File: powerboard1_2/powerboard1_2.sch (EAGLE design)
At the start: 132 parts, among them Q1 IPP80P03P4L04AKSA1, Q2 2N4401TFR, Q3 2N4401TFR, Q4 2N4401TFR, U1 UWQ-12/20-T48NTB-C, U2 UWE-5/20-Q48NB-C, U3 UWE-3.3/30-Q48NB-C

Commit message: Changed converters to ones that have input voltage range of 9V to 36V; Reduced length by about 0.5"
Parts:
- U1: value UWQ-12/20-T48NTB-C -> UWE-12/10-Q12PB-C; device New Power Board Library:UWQ-12/20-T48NTB-C -> New Power Board Library:UWE-12/10-Q12PB-C
- U2: value UWE-5/20-Q48NB-C -> UWE-5/15-Q12PB-C; device New Power Board Library:UWE-5/20-Q48NB-C -> New Power Board Library:UWE-5/15-Q12PB-C
- U3: value UWE-3.3/30-Q48NB-C -> UWE-3.3/20-Q12PB-C; device New Power Board Library:UWE-3.3/30-Q48NB-C -> New Power Board Library:UWE-3.3/20-Q12PB-C
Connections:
- new net N$15: U3.+VIN
- net 12V+SENSE: now also R5.1; no longer R11.2
- net 12V-SENSE: now also JP8.5, JP8.6, R13.2, U1.+SEN; no longer JP8.1, JP8.2, R3.1, U1.+SENSE
- net 3V3+SENSE: now also R3.1; no longer R13.2
- net 3V3-SENSE: now also JP8.1, JP8.2, R11.2; no longer JP8.5, JP8.6, R5.1
- net 5V+SENSE: now also R4.1; no longer R12.2
- net 5V-SENSE: now also R12.2; no longer R4.1
- net GND: now also U1.-SEN; no longer U1.-SENSE
- net N$12: no longer U3.+VIN

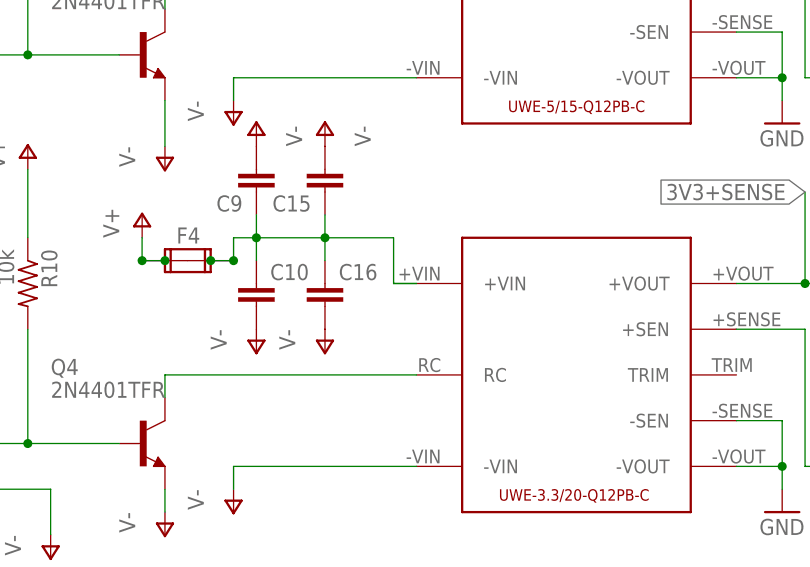
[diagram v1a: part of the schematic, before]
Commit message: Fixed connection issue on 3.3V converter
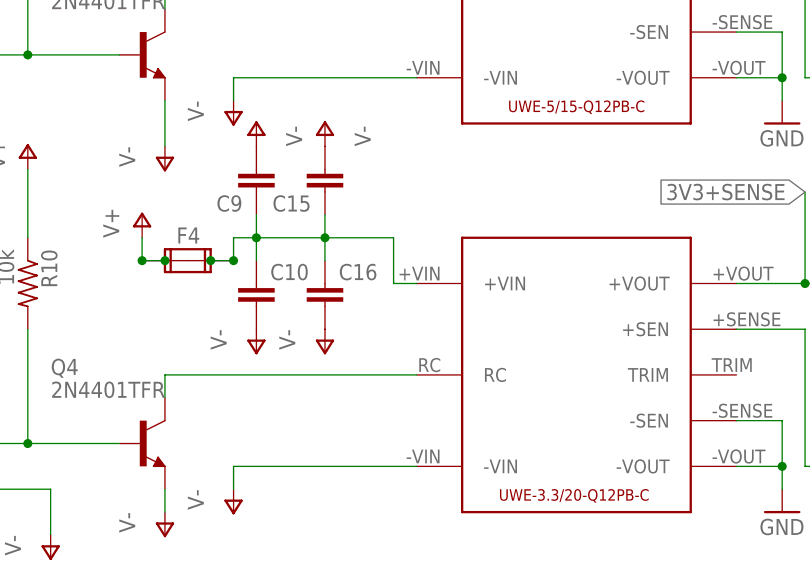
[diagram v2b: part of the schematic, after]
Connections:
- removed net N$15: U3.+VIN
- net N$12: now also U3.+VIN
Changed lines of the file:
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@@
-</segment>
-</net>
-<net name="N$15" class="0">
-<segment>
-<wire x1="116.84" y1="154.94" x2="119.38" y2="154.94" width="0.1524" layer="91"/>
-<pinref part="U3" gate="G$1" pin="+VIN"/>
 </segment>
 </net>
@@
 <wire x1="101.6" y1="160.02" x2="109.22" y2="160.02" width="0.1524" layer="91"/>
 <wire x1="109.22" y1="160.02" x2="116.84" y2="160.02" width="0.1524" layer="91"/>
-<wire x1="116.84" y1="154.94" x2="119.38" y2="154.94" width="0.1524" layer="91"/>
 <wire x1="116.84" y1="160.02" x2="116.84" y2="154.94" width="0.1524" layer="91"/>
 <pinref part="C9" gate="G$1" pin="1"/>
@@
 <junction x="109.22" y="160.02"/>
 <junction x="99.06" y="157.48"/>
+<pinref part="U3" gate="G$1" pin="+VIN"/>
+<wire x1="116.84" y1="154.94" x2="119.38" y2="154.94" width="0.1524" layer="91"/>
 </segment>
 </net>

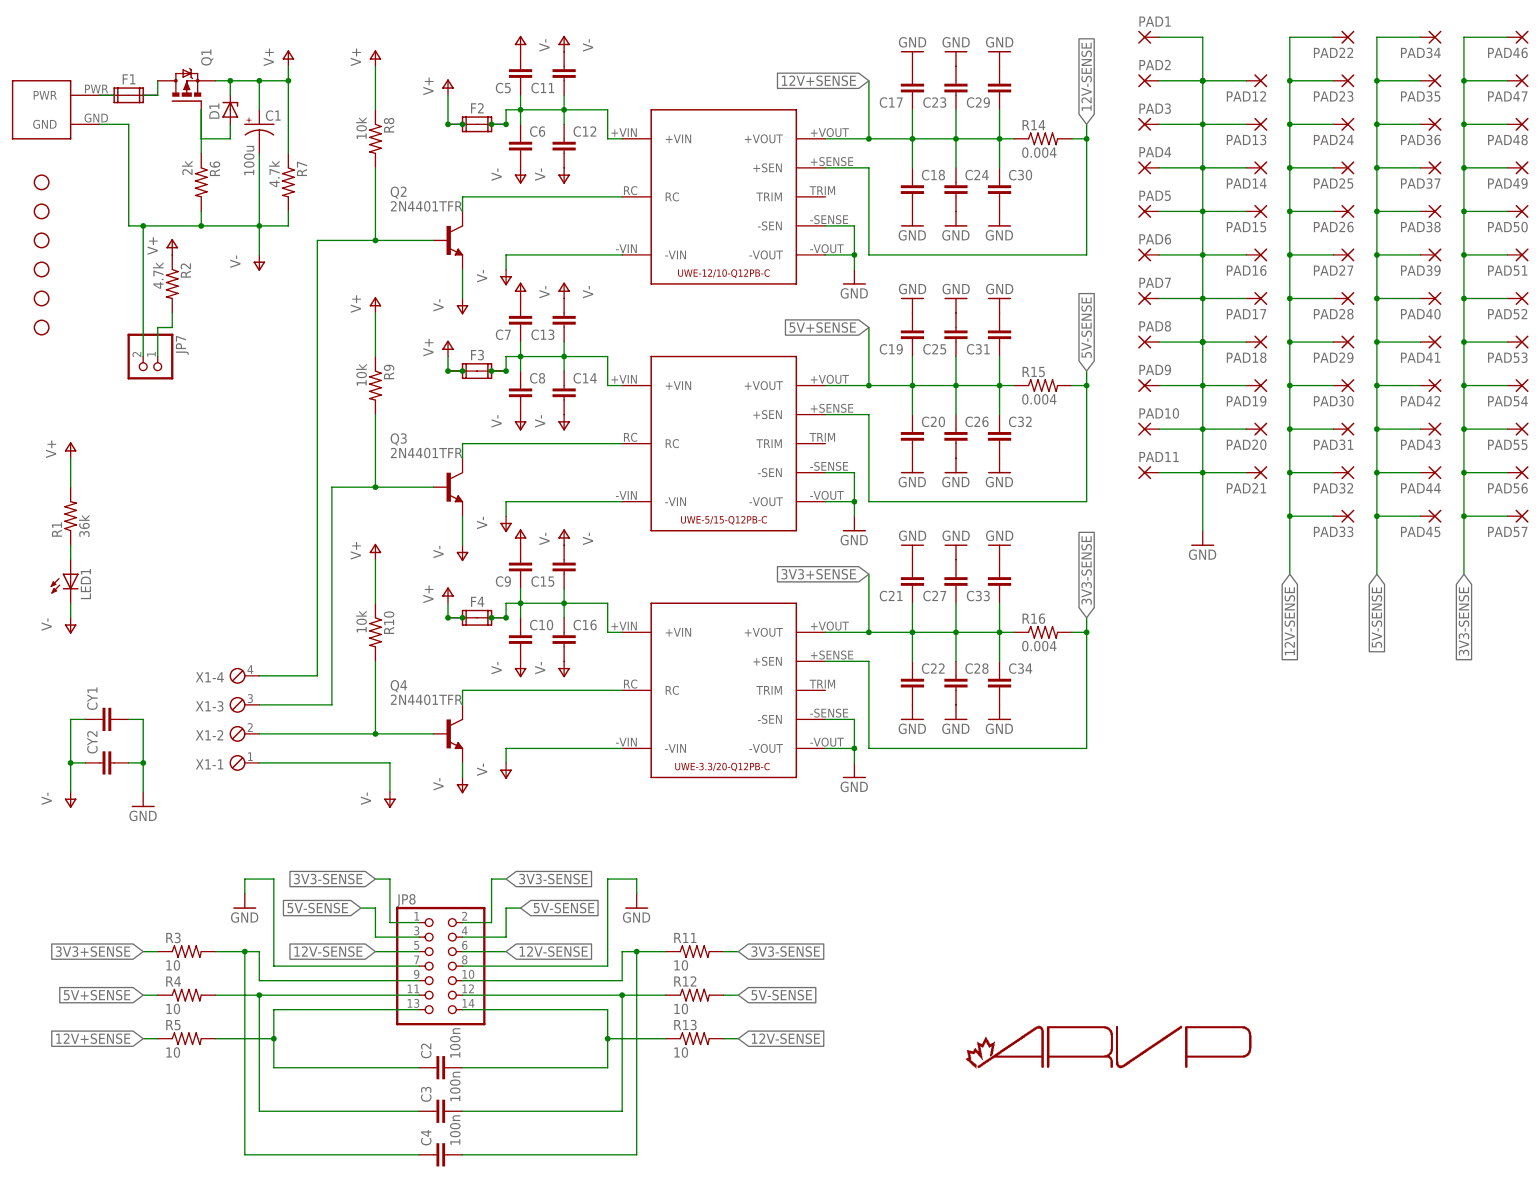
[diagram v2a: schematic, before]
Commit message: Added 2 pin header for global on/off switch; Changed on/off terminal block to 2x3 90 degree pin header; Added LED indicators on each rail; Reduced number of output wire pads; Changed battery connection to screw terminal
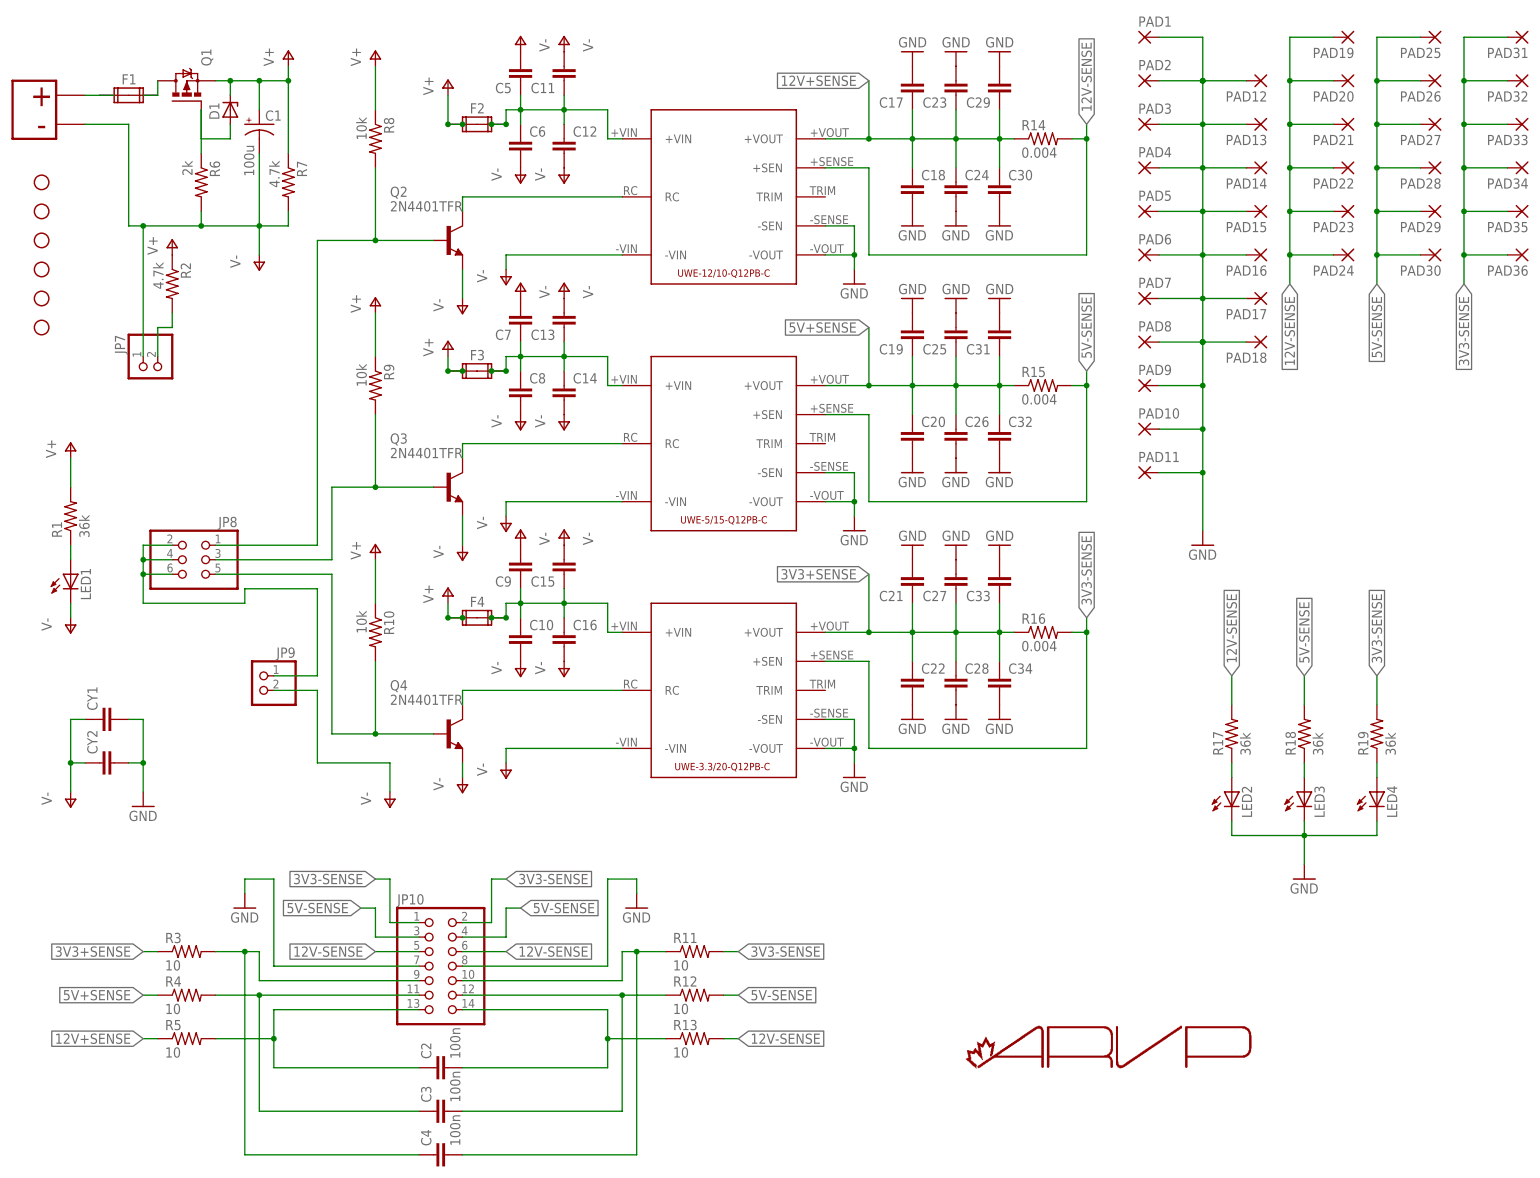
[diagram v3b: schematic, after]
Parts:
- removed P$1: AND_PWR, ARVP:AND_PWR
- removed PAD37, PAD38, PAD39, PAD40, PAD41, PAD42, PAD43, PAD44, PAD45, PAD46, PAD47, PAD48, PAD49, PAD50, PAD51, PAD52, PAD53, PAD54, PAD55, PAD56, PAD57: WIREPAD3,17/1,3, wirepad:WIREPAD3,17/1,3
- removed X1: (no value), con-phoenix-254:MPT4
- added JP10: (no value), pinhead:PINHD-2X7
- added JP9: (no value), pinhead:PINHD-1X2/90
- added LED2, LED3, LED4: (no value), led:LED3MM
- added R17, R18, R19: 36k, resistor:R-US_0204/7
- added T1: 2_POS_TERMINAL, New Power Board Library:2_POS_TERMINAL
- JP7: device pinhead:PINHD-1X2 -> pinhead:PINHD-1X2/90
- JP8: device pinhead:PINHD-2X7 -> pinhead:PINHD-2X3/90
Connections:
- net N$10 renamed ENABLE_5V
- net N$11 renamed ENABLE_3V3
- net N$8 renamed ENABLE_12V
- new net N$10: LED3.A, R18.1
- new net N$11: LED4.A, R19.1
- new net N$8: JP8.2, JP8.4, JP8.6, JP9.1
- new net N$9: LED2.A, R17.1
- net 12V-SENSE: now also JP10.5, JP10.6, PAD19.P, PAD20.P, PAD21.P, R17.2; no longer JP8.5, JP8.6, PAD25.P, PAD26.P, PAD27.P, PAD28.P, PAD29.P, PAD30.P, PAD31.P, PAD32.P, PAD33.P
- net 3V3-SENSE: now also JP10.1, JP10.2, PAD31.P, PAD32.P, PAD33.P, PAD34.P, PAD35.P, PAD36.P, R19.2; no longer JP8.1, JP8.2, PAD46.P, PAD47.P, PAD48.P, PAD49.P, PAD50.P, PAD51.P, PAD52.P, PAD53.P, PAD54.P, PAD55.P, PAD56.P, PAD57.P
- net 5V-SENSE: now also JP10.3, JP10.4, PAD25.P, PAD26.P, PAD27.P, PAD28.P, PAD29.P, PAD30.P, R18.2; no longer JP8.3, JP8.4, PAD34.P, PAD35.P, PAD36.P, PAD37.P, PAD38.P, PAD39.P, PAD40.P, PAD41.P, PAD42.P, PAD43.P, PAD44.P, PAD45.P
- net GND: now also JP10.7, JP10.8, LED2.C, LED3.C, LED4.C; no longer JP8.7, JP8.8, PAD19.P, PAD20.P, PAD21.P
- net J3: now also JP10.9; no longer JP8.9
- net J4: now also JP10.10; no longer JP8.10
- net J5: now also JP10.11; no longer JP8.11
- net J6: now also JP10.12; no longer JP8.12
- net J7: now also JP10.13; no longer JP8.13
- net J8: now also JP10.14; no longer JP8.14
- net N$2: now also JP7.2; no longer JP7.1
- net N$3: now also T1.P$1; no longer P$1.PWR
- net ON/OFF_1: now also JP8.1; no longer X1-4.1
- net ON/OFF_2: now also JP8.3; no longer X1-3.1
- net ON/OFF_3: now also JP8.5; no longer X1-2.1
- net V-: now also JP7.1, JP9.2, T1.P$2; no longer JP7.2, P$1.GND, X1-1.1
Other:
- moved on the sheet: PAD19, PAD20, PAD21, PAD22, PAD23, PAD24, PAD25, PAD26, PAD27, PAD28, PAD29, PAD30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
